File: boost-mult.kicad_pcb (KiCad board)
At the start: 2 copper layers, 19 x 100 mm, 29 parts, among them J1 IN, J2 OUT1, J3 OUT2, J4 OUT3, J5 OUT4, J6 PWR, SW1 AC_COUPLE, SW2 DRIVE, U1 TL074, U2 TL072

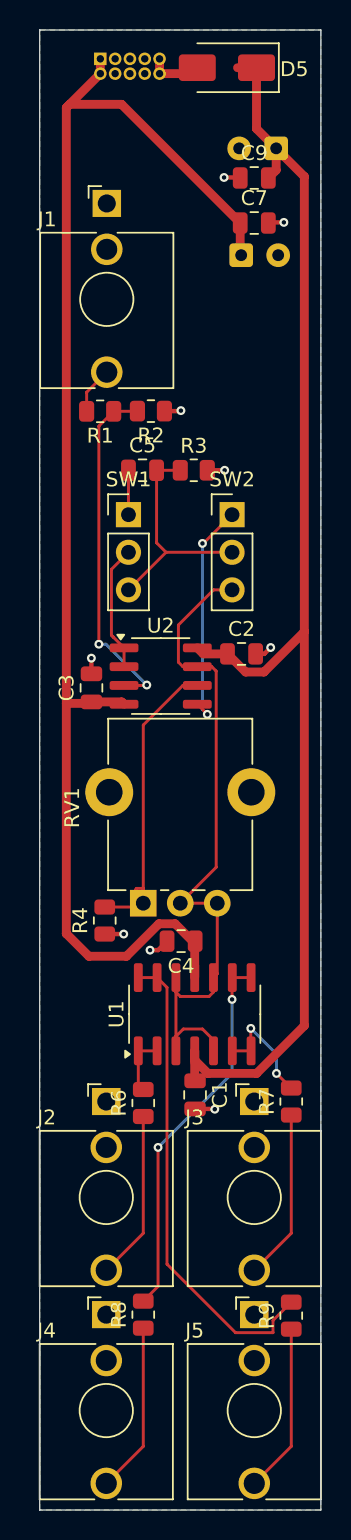
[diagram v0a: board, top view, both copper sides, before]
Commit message: jack layout, top layer gnd, vias
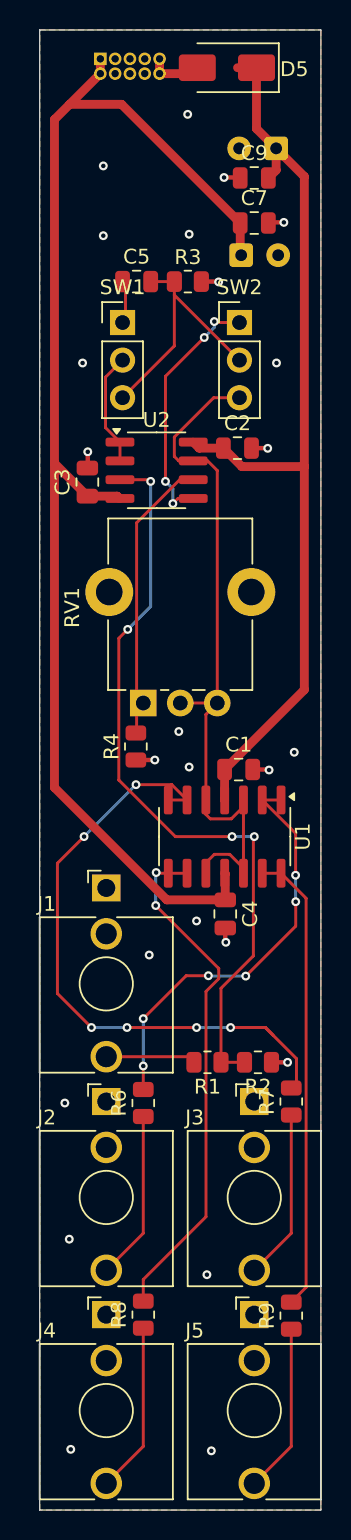
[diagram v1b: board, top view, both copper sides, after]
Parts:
- moved J1 46.3 mm to (124.5, 118.0)
- moved R2 44.6 mm to (134.8, 129.8)
- moved R1 44.6 mm to (131.3, 129.8)
- moved C1 22.2 mm to (133.4, 110.0), turned to 0 degrees
- moved C3 13.9 mm to (123.2, 90.5)
- moved C2 13.9 mm to (133.4, 88.3)
- moved U2 13.9 mm to (127.9, 89.8)
- moved RV1 13.5 mm to (127.0, 105.5)
- moved SW2 13.0 mm to (133.5, 79.8)
- moved SW1 13.0 mm to (125.6, 79.8)
- moved C5 12.8 mm to (126.5, 77.0)
- moved R3 12.8 mm to (130.0, 77.0)
- moved U1 12.2 mm to (132.5, 114.5), turned to -90 degrees
- moved R4 11.9 mm to (126.5, 108.4)
- moved C4 3.51 mm to (132.5, 119.7), turned to -90 degrees
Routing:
- net Net-(U1B--): track 7.96 -> 45.3 mm, vias 2 -> 6
- net Net-(U2A-+): track 23.7 -> 51.7 mm, vias 2 -> 4
- net +12V: track 91.2 -> 65.6 mm
- net Net-(U1A--): track 4.02 -> 28.4 mm, vias 0 -> 6
- net Net-(U1C--): track 25.6 -> 35.0 mm
- net -12V: track 94.2 -> 89.5 mm
- net Net-(J1-PadT): track 3.21 -> 6.08 mm
- net Net-(SW2-A): track 15.4 -> 17.1 mm, vias 2 -> 4
- net Net-(SW1-C): track 15.5 -> 17.1 mm
- net Net-(U1D--): track 32.6 -> 31.4 mm
- net Net-(SW1-B): track 8.60 -> 7.69 mm
- net Net-(U2B--): track 20.1 -> 19.3 mm
- net GND: track 11.3 -> 10.6 mm, vias 9 -> 25
- added copper zone on F.Cu, net GND

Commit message: tweak top gnd pour
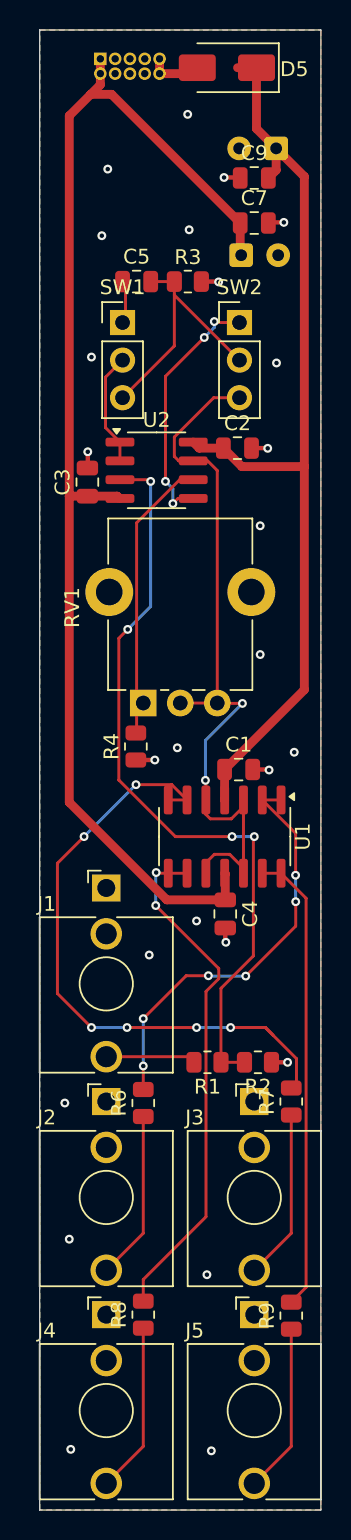
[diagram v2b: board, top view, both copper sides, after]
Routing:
- net -12V: track 89.5 -> 85.6 mm
- net Net-(SW2-C): track 48.8 -> 51.2 mm, vias 0 -> 2
- net GND: vias 25 -> 26
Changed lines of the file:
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@@
 	)
 	(via
-		(at 129.4 107.4)
+		(at 129.3 108.5)
 		(size 0.6)
 		(drill 0.3)
@@
 	)
 	(via
-		(at 130.1 73.8)
-		(size 0.6)
-		(drill 0.3)
-		(layers "F.Cu" "B.Cu")
-		(free yes)
-		(net 1)
-	)
-	(via
-		(at 130.1 109.8)
+		(at 130.1 73.5)
+		(size 0.6)
+		(drill 0.3)
+		(layers "F.Cu" "B.Cu")
+		(free yes)
+		(net 1)
+	)
+	(via
+		(at 134.9 102.2)
 		(size 0.6)
 		(drill 0.3)
@@
 	)
 	(via
-		(at 124.3 73.9)
+		(at 124.2 73.9)
 		(size 0.6)
 		(drill 0.3)
@@
 	)
 	(via
-		(at 122.9 82.5)
+		(at 123.5 82.1)
 		(size 0.6)
 		(drill 0.3)
@@
 	)
 	(via
-		(at 124.3 69.184901)
+		(at 124.6 69.4)
 		(size 0.6)
 		(drill 0.3)
@@
 	(via
 		(at 131.6 156)
+		(size 0.6)
+		(drill 0.3)
+		(layers "F.Cu" "B.Cu")
+		(free yes)
+		(net 1)
+	)
+	(via
+		(at 134.9 93.5)
 		(size 0.6)
 		(drill 0.3)
@@
 	)
 	(segment
-		(start 122.025 65.025)
-		(end 121 66.05)
-		(width 0.6)
-		(layer "F.Cu")
-		(net 3)
-	)
-	(segment
 		(start 133.55 73.042968)
 		(end 133.55 75.151869)
@@
 	)
 	(segment
+		(start 122 112.18481)
+		(end 128.59019 118.775)
+		(width 0.6)
+		(layer "F.Cu")
+		(net 3)
+	)
+	(segment
+		(start 123.45 64.35)
+		(end 124.857032 64.35)
+		(width 0.6)
+		(layer "F.Cu")
+		(net 3)
+	)
+	(segment
 		(start 123.223662 91.497277)
 		(end 125.241277 91.497277)
@@
 	)
 	(segment
-		(start 122.025 65.025)
-		(end 125.532032 65.025)
-		(width 0.6)
-		(layer "F.Cu")
-		(net 3)
-	)
-	(segment
-		(start 121 111.18481)
-		(end 128.59019 118.775)
+		(start 123.45 64.35)
+		(end 122 65.8)
+		(width 0.6)
+		(layer "F.Cu")
+		(net 3)
+	)
+	(segment
+		(start 128.59019 118.775)
+		(end 132.54 118.775)
 		(width 0.6)
 		(layer "F.Cu")
@@
 	)
 	(segment
-		(start 121 66.05)
-		(end 121 89.273615)
-		(width 0.6)
-		(layer "F.Cu")
-		(net 3)
-	)
-	(segment
-		(start 121 89.273615)
-		(end 121 111.18481)
+		(start 122 65.8)
+		(end 122 91.5)
+		(width 0.6)
+		(layer "F.Cu")
+		(net 3)
+	)
+	(segment
+		(start 122 91.5)
+		(end 122 112.18481)
+		(width 0.6)
+		(layer "F.Cu")
+		(net 3)
+	)
+	(segment
+		(start 124.857032 64.35)
+		(end 133.55 73.042968)
+		(width 0.6)
+		(layer "F.Cu")
+		(net 3)
+	)
+	(segment
+		(start 124.1 62.95)
+		(end 124.1 63.7)
+		(width 0.6)
+		(layer "F.Cu")
+		(net 3)
+	)
+	(segment
+		(start 124.1 63.7)
+		(end 123.45 64.35)
+		(width 0.6)
+		(layer "F.Cu")
+		(net 3)
+	)
+	(segment
+		(start 122 91.5)
+		(end 122.002723 91.497277)
 		(width 0.6)
 		(layer "F.Cu")
@@
 	)
 	(segment
-		(start 124.1 62.95)
-		(end 122.025 65.025)
-		(width 0.6)
-		(layer "F.Cu")
-		(net 3)
-	)
-	(segment
-		(start 121 89.273615)
-		(end 123.223662 91.497277)
-		(width 0.6)
-		(layer "F.Cu")
-		(net 3)
-	)
-	(segment
-		(start 128.59019 118.775)
-		(end 132.54 118.775)
-		(width 0.6)
-		(layer "F.Cu")
-		(net 3)
-	)
-	(segment
 		(start 133.55 75.151869)
 		(end 133.614344 75.216213)
@@
 	)
 	(segment
-		(start 125.532032 65.025)
-		(end 133.55 73.042968)
-		(width 0.6)
-		(layer "F.Cu")
-		(net 3)
-	)
-	(segment
 		(start 124.1 61.95)
 		(end 124.1 62.95)
@@
 		(start 132.54 117.015)
 		(end 132.5 116.975)
+		(width 0.6)
+		(layer "F.Cu")
+		(net 3)
+	)
+	(segment
+		(start 122.002723 91.497277)
+		(end 123.223662 91.497277)
 		(width 0.6)
 		(layer "F.Cu")
@@
 	)
 	(segment
+		(start 131.23 112.025)
+		(end 131.23 110.73)
+		(width 0.2)
+		(layer "F.Cu")
+		(net 14)
+	)
+	(segment
 		(start 133.77 116.628032)
 		(end 132.840968 115.699)
@@
 	)
 	(segment
+		(start 133.7 105.5)
+		(end 132.025 105.5)
+		(width 0.2)
+		(layer "F.Cu")
+		(net 14)
+	)
+	(segment
 		(start 133.77 112.025)
 		(end 133.77 116.975)
@@
 	)
 	(segment
+		(start 131.23 110.73)
+		(end 131.2 110.7)
+		(width 0.2)
+		(layer "F.Cu")
+		(net 14)
+	)
+	(segment
 		(start 130.375 89.115)
 		(end 131.349999 89.115)
@@
 	)
 	(segment
-		(start 131.23 106.245)
-		(end 131.23 112.025)
-		(width 0.2)
-		(layer "F.Cu")
-		(net 14)
-	)
-	(segment
-		(start 132 105.475)
-		(end 131.23 106.245)
-		(width 0.2)
-		(layer "F.Cu")
-		(net 14)
-	)
-	(segment
 		(start 129.400001 89.115)
 		(end 130.375 89.115)
@@
 	)
 	(segment
+		(start 132.025 105.5)
+		(end 132 105.475)
+		(width 0.2)
+		(layer "F.Cu")
+		(net 14)
+	)
+	(segment
 		(start 131.349999 89.115)
 		(end 132 89.765001)
@@
 		(net 14)
 	)
+	(via
+		(at 133.7 105.5)
+		(size 0.6)
+		(drill 0.3)
+		(layers "F.Cu" "B.Cu")
+		(net 14)
+	)
+	(via
+		(at 131.2 110.7)
+		(size 0.6)
+		(drill 0.3)
+		(layers "F.Cu" "B.Cu")
+		(net 14)
+	)
+	(segment
+		(start 131.2 108)
+		(end 133.7 105.5)
+		(width 0.2)
+		(layer "B.Cu")
+		(net 14)
+	)
+	(segment
+		(start 131.2 110.7)
+		(end 131.2 108)
+		(width 0.2)
+		(layer "B.Cu")
+		(net 14)
+	)
